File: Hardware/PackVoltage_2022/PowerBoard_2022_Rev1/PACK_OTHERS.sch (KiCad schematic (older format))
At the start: 20 parts, among them Q1 BUK7M8R5-40HX, Q2 BUK7M8R5-40HX, U1 LT1910, U2 INA281, U3 LT1910, U4 INA281

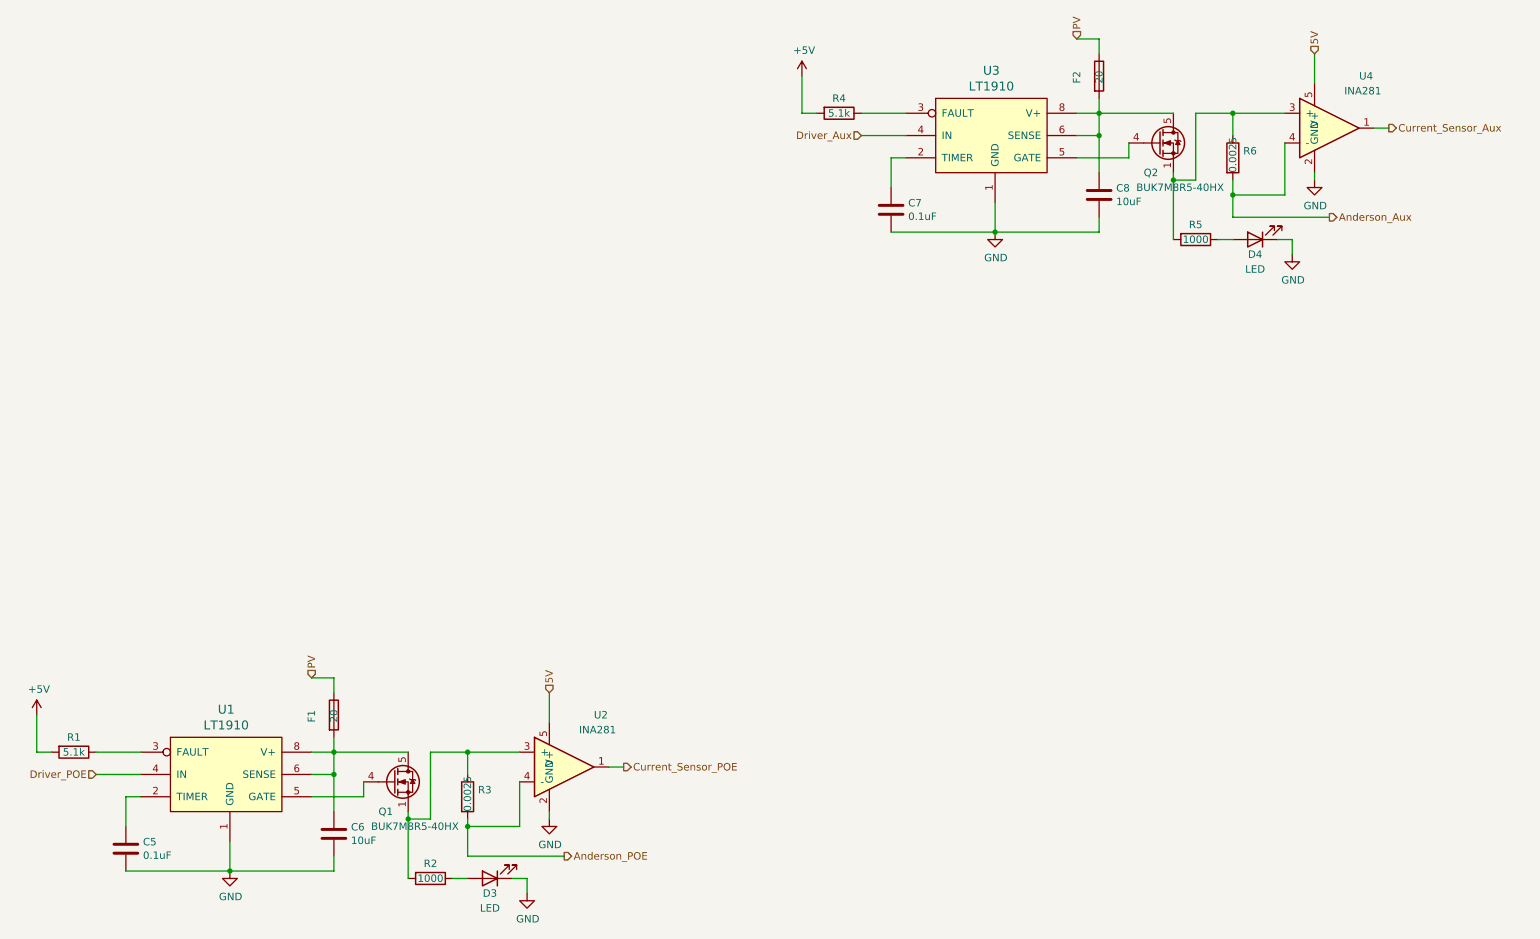
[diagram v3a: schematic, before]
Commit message: Organized  Stuff into groups and changed how we organize our board
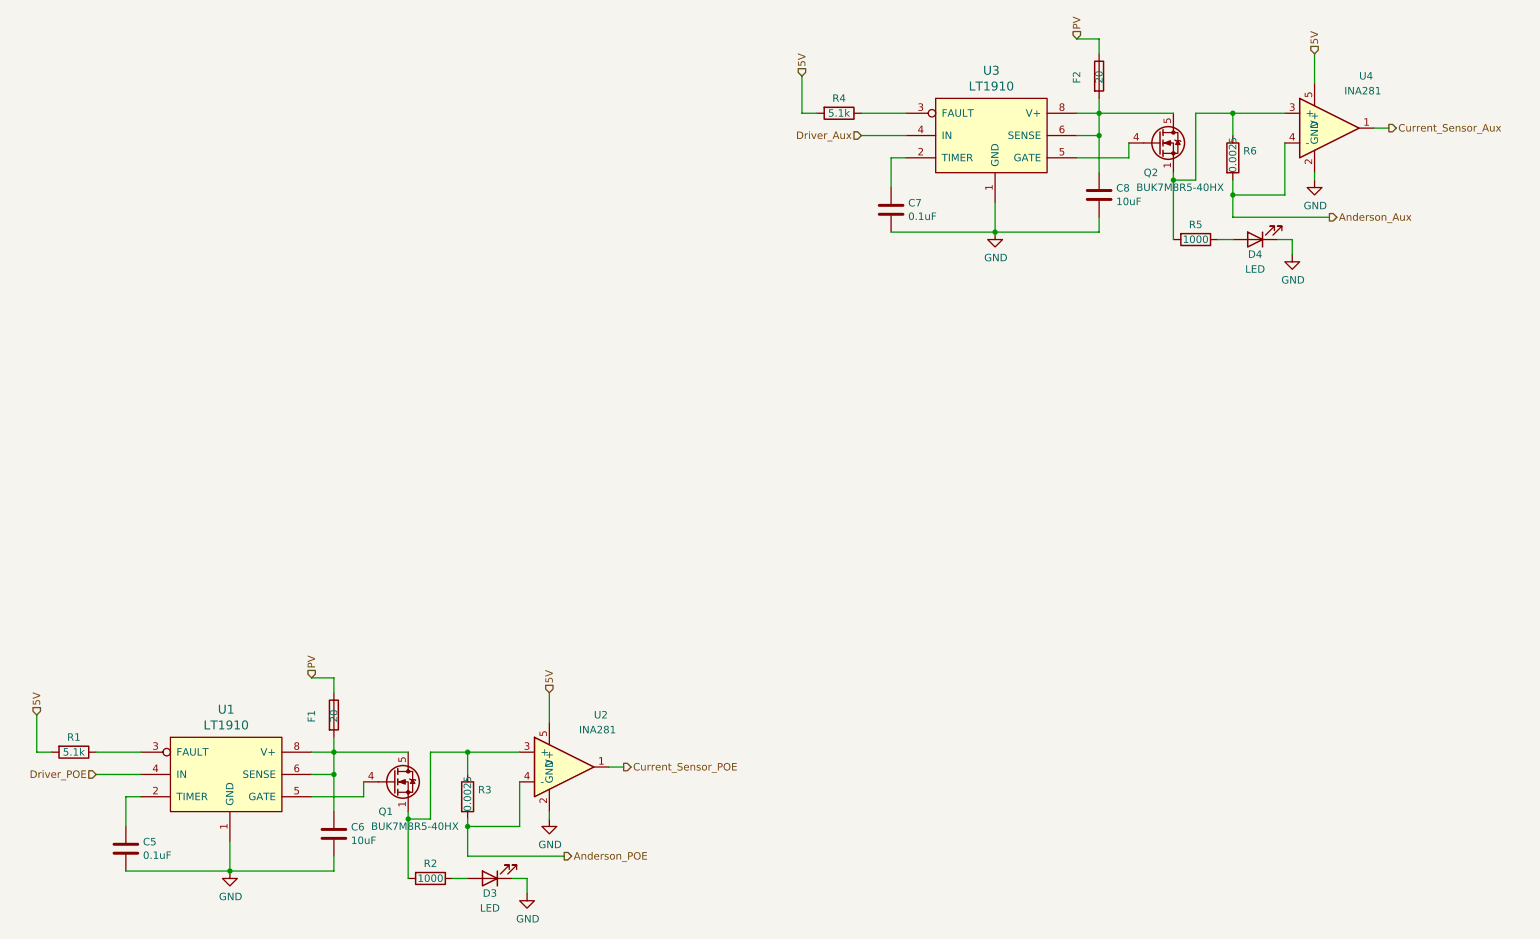
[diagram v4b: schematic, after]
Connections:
- net +5V is gone; now on net 5V: R1.2, R4.2
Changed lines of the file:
@@
 EESchema Schematic File Version 4
-EELAYER 30 0
+LIBS:PowerBoard_2022_Rev1-cache
+EELAYER 26 0
 EELAYER END
 $Descr A4 11693 8268
@@
 Wire Wire Line
 	6650 1700 6950 1700
-$Comp
-L power:+5V #PWR?
-U 1 1 61612B20
-P 6250 1450
-AR Path="/615D5992/61612B20" Ref="#PWR?"  Part="1"
-AR Path="/61609A41/61612B20" Ref="#PWR06"  Part="1"
-F 0 "#PWR06" H 6250 1300 50  0001 C CNN
-F 1 "+5V" H 6265 1623 50  0000 C CNN
-F 2 "" H 6250 1450 50  0001 C CNN
-F 3 "" H 6250 1450 50  0001 C CNN
-	1    6250 1450
-	1    0    0    -1
-$EndComp
 Wire Wire Line
 	6250 1450 6250 1700
@@
 Wire Wire Line
 	1500 6000 1800 6000
-$Comp
-L power:+5V #PWR?
-U 1 1 616288B7
-P 1100 5750
-AR Path="/615D5992/616288B7" Ref="#PWR?"  Part="1"
-AR Path="/61609A41/616288B7" Ref="#PWR02"  Part="1"
-F 0 "#PWR02" H 1100 5600 50  0001 C CNN
-F 1 "+5V" H 1115 5923 50  0000 C CNN
-F 2 "" H 1100 5750 50  0001 C CNN
-F 3 "" H 1100 5750 50  0001 C CNN
-	1    1100 5750
-	1    0    0    -1
-$EndComp
 Wire Wire Line
 	1100 5750 1100 6000
@@
 Wire Wire Line
 	9150 2250 9150 2400
+Text HLabel 1100 5750 1    50   Input ~ 0
+5V
+Text HLabel 6250 1450 1    50   Input ~ 0
+5V
 $EndSCHEMATC

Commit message: Replaced 12v okis w/big buck. Changed .0025 resistors to not 603.
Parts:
- R3, R6: footprint Resistor_SMD:R_0603_1608Metric_Pad1.05x0.95mm_HandSolder -> Resistor_SMD:R_1206_3216Metric_Pad1.30x1.75mm_HandSolder
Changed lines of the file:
@@
 EESchema Schematic File Version 4
-LIBS:PowerBoard_2022_Rev1-cache
-EELAYER 26 0
+EELAYER 30 0
 EELAYER END
 $Descr A4 11693 8268
@@
 F 0 "R6" H 9220 2046 50  0000 L CNN
 F 1 "0.0025" V 9150 1900 50  0000 L CNN
-F 2 "Resistor_SMD:R_0603_1608Metric_Pad1.05x0.95mm_HandSolder" V 9080 2000 50  0001 C CNN
+F 2 "Resistor_SMD:R_1206_3216Metric_Pad1.30x1.75mm_HandSolder" V 9080 2000 50  0001 C CNN
 F 3 "~" H 9150 2000 50  0001 C CNN
 	1    9150 2000
@@
 F 0 "R3" H 4070 6346 50  0000 L CNN
 F 1 "0.0025" V 4000 6200 50  0000 L CNN
-F 2 "Resistor_SMD:R_0603_1608Metric_Pad1.05x0.95mm_HandSolder" V 3930 6300 50  0001 C CNN
+F 2 "Resistor_SMD:R_1206_3216Metric_Pad1.30x1.75mm_HandSolder" V 3930 6300 50  0001 C CNN
 F 3 "~" H 4000 6300 50  0001 C CNN
 	1    4000 6300
